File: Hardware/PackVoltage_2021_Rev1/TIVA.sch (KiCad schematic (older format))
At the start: 1 part, among them U24 TM4C129E_Launchpad

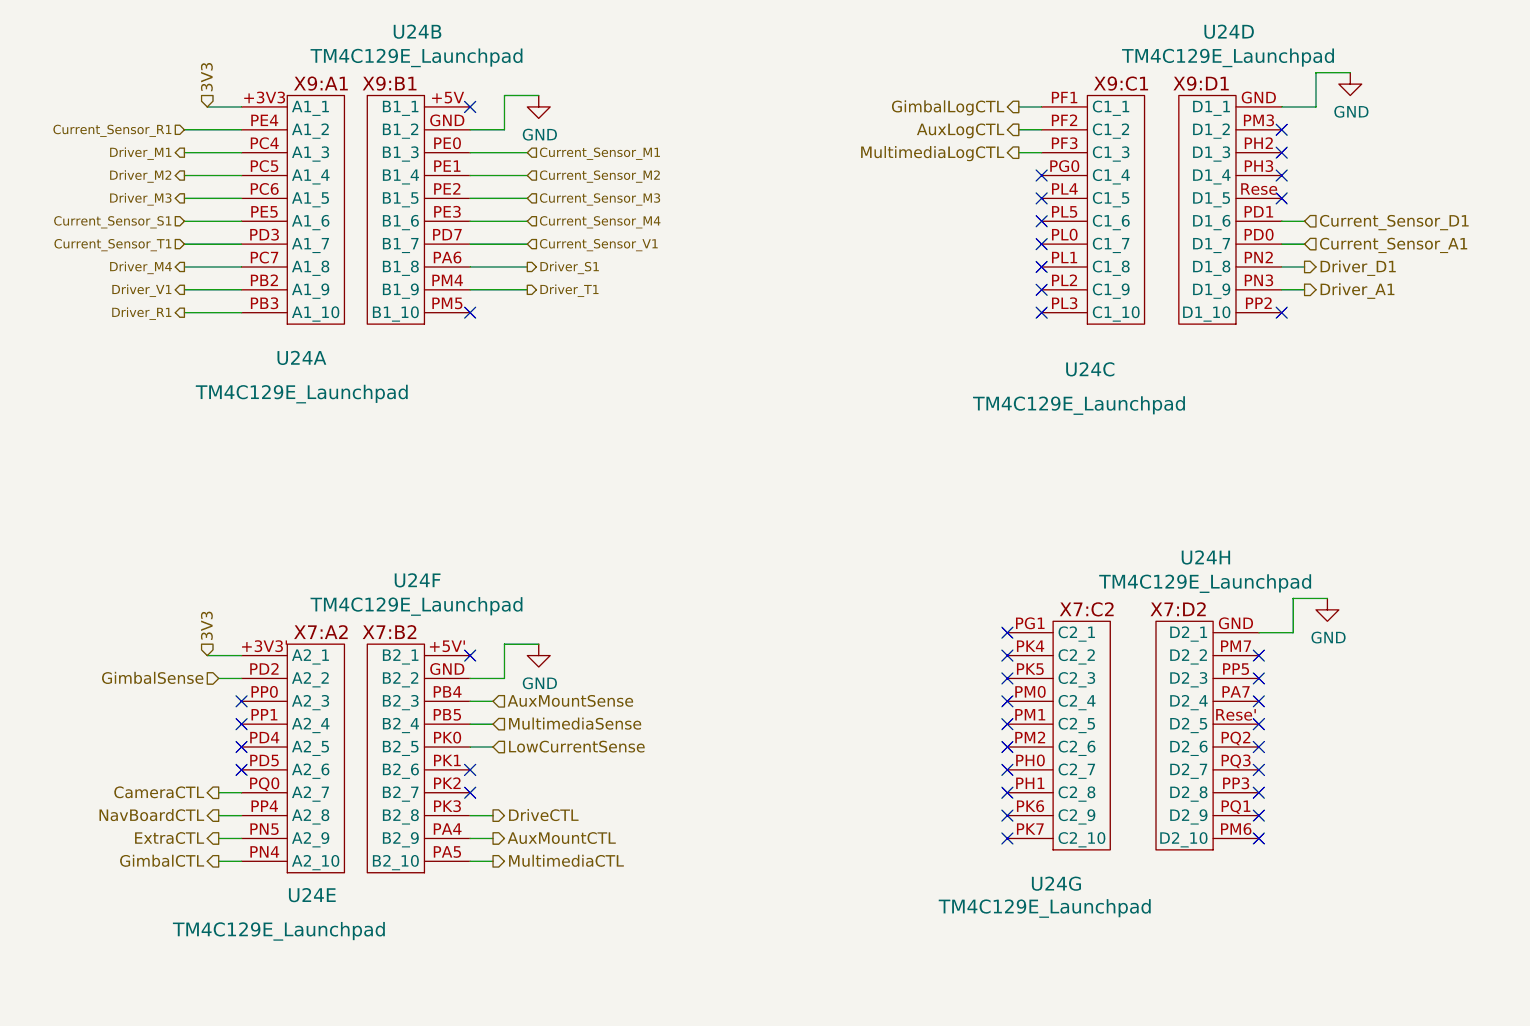
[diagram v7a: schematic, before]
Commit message: Rearranged Tiva Pins
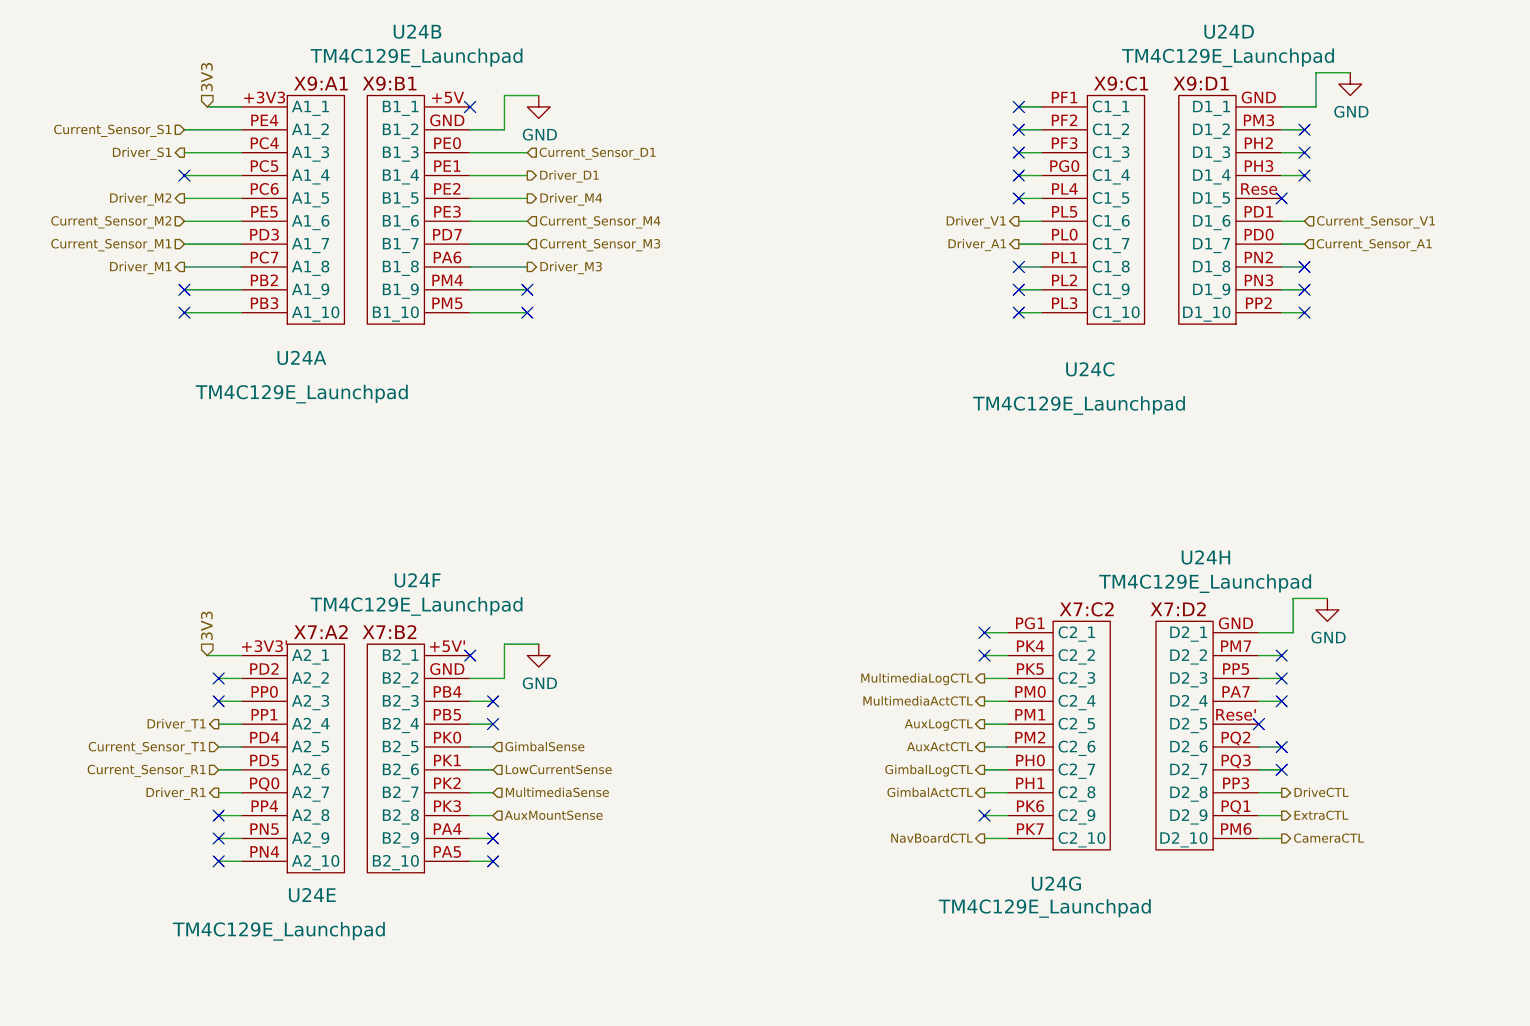
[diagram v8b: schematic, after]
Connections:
- net AuxLogCTL: now also U24.PM1 (C2_5); no longer U24.PF2 (C1_2)
- net AuxMountSense: now also U24.PK3 (B2_8); no longer U24.PB4 (B2_3)
- net CameraCTL: now also U24.PM6 (D2_10); no longer U24.PQ0 (A2_7)
- net Current_Sensor_D1: now also U24.PE0 (B1_3); no longer U24.PD1 (D1_6)
- net Current_Sensor_M1: now also U24.PD3 (A1_7); no longer U24.PE0 (B1_3)
- net Current_Sensor_M2: now also U24.PE5 (A1_6); no longer U24.PE1 (B1_4)
- net Current_Sensor_M3: now also U24.PD7 (B1_7); no longer U24.PE2 (B1_5)
- net Current_Sensor_R1: now also U24.PD5 (A2_6); no longer U24.PE4 (A1_2)
- net Current_Sensor_S1: now also U24.PE4 (A1_2); no longer U24.PE5 (A1_6)
- net Current_Sensor_T1: now also U24.PD4 (A2_5); no longer U24.PD3 (A1_7)
- net Current_Sensor_V1: now also U24.PD1 (D1_6); no longer U24.PD7 (B1_7)
- net DriveCTL: now also U24.PP3 (D2_8); no longer U24.PK3 (B2_8)
- net Driver_A1: now also U24.PL0 (C1_7); no longer U24.PN3 (D1_9)
- net Driver_D1: now also U24.PE1 (B1_4); no longer U24.PN2 (D1_8)
- net Driver_M1: now also U24.PC7 (A1_8); no longer U24.PC4 (A1_3)
- net Driver_M2: now also U24.PC6 (A1_5); no longer U24.PC5 (A1_4)
- net Driver_M3: now also U24.PA6 (B1_8); no longer U24.PC6 (A1_5)
- net Driver_M4: now also U24.PE2 (B1_5); no longer U24.PC7 (A1_8)
- net Driver_R1: now also U24.PQ0 (A2_7); no longer U24.PB3 (A1_10)
- net Driver_S1: now also U24.PC4 (A1_3); no longer U24.PA6 (B1_8)
- net Driver_T1: now also U24.PP1 (A2_4); no longer U24.PM4 (B1_9)
- net Driver_V1: now also U24.PL5 (C1_6); no longer U24.PB2 (A1_9)
- net ExtraCTL: now also U24.PQ1 (D2_9); no longer U24.PN5 (A2_9)
- net GimbalLogCTL: now also U24.PH0 (C2_7); no longer U24.PF1 (C1_1)
- net GimbalSense: now also U24.PK0 (B2_5); no longer U24.PD2 (A2_2)
- net LowCurrentSense: now also U24.PK1 (B2_6); no longer U24.PK0 (B2_5)
- net MultimediaLogCTL: now also U24.PK5 (C2_3); no longer U24.PF3 (C1_3)
- net MultimediaSense: now also U24.PK2 (B2_7); no longer U24.PB5 (B2_4)
- net NavBoardCTL: now also U24.PK7 (C2_10); no longer U24.PP4 (A2_8)
- net GimbalActCTL: now reaches U24.PH1 (C2_8)
- net MultimediaActCTL: now reaches U24.PM0 (C2_4)
- net AuxActCTL: now reaches U24.PM2 (C2_6)
- net AuxMountCTL: no longer names the net of U24.PA4 (B2_9)
- net GimbalCTL: no longer names the net of U24.PN4 (A2_10)
- net MultimediaCTL: no longer names the net of U24.PA5 (B2_10)
